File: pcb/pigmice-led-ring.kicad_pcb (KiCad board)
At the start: 2 copper layers, 65 x 56 mm, 37 parts, among them J1 Conn_02x20_Odd_Even, J2 Conn_01x02_Female, U1 TPS61165, U2 LMR33630

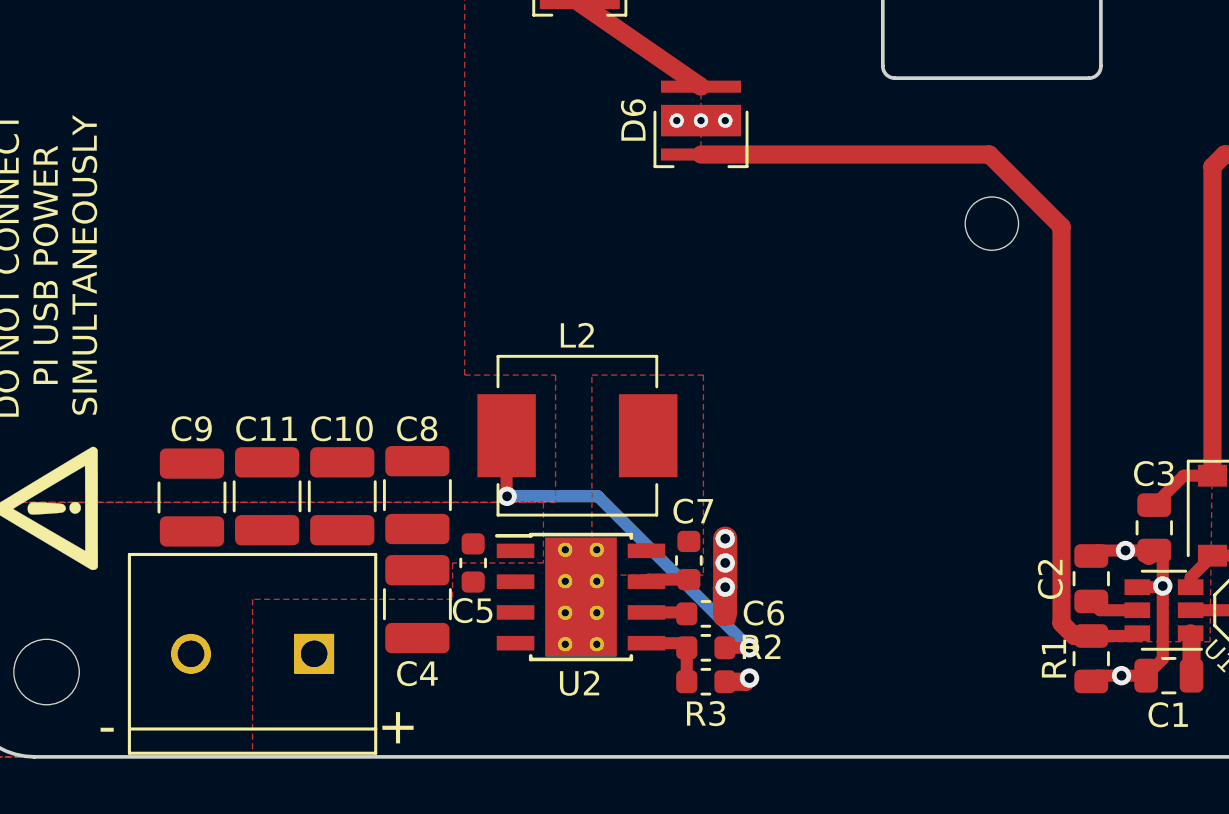
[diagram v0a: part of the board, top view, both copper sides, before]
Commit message: Cleanup PCB
- Order 5v output capacitors
- Don't show J1 and J2 footprints
- Add OSHW logo to the back
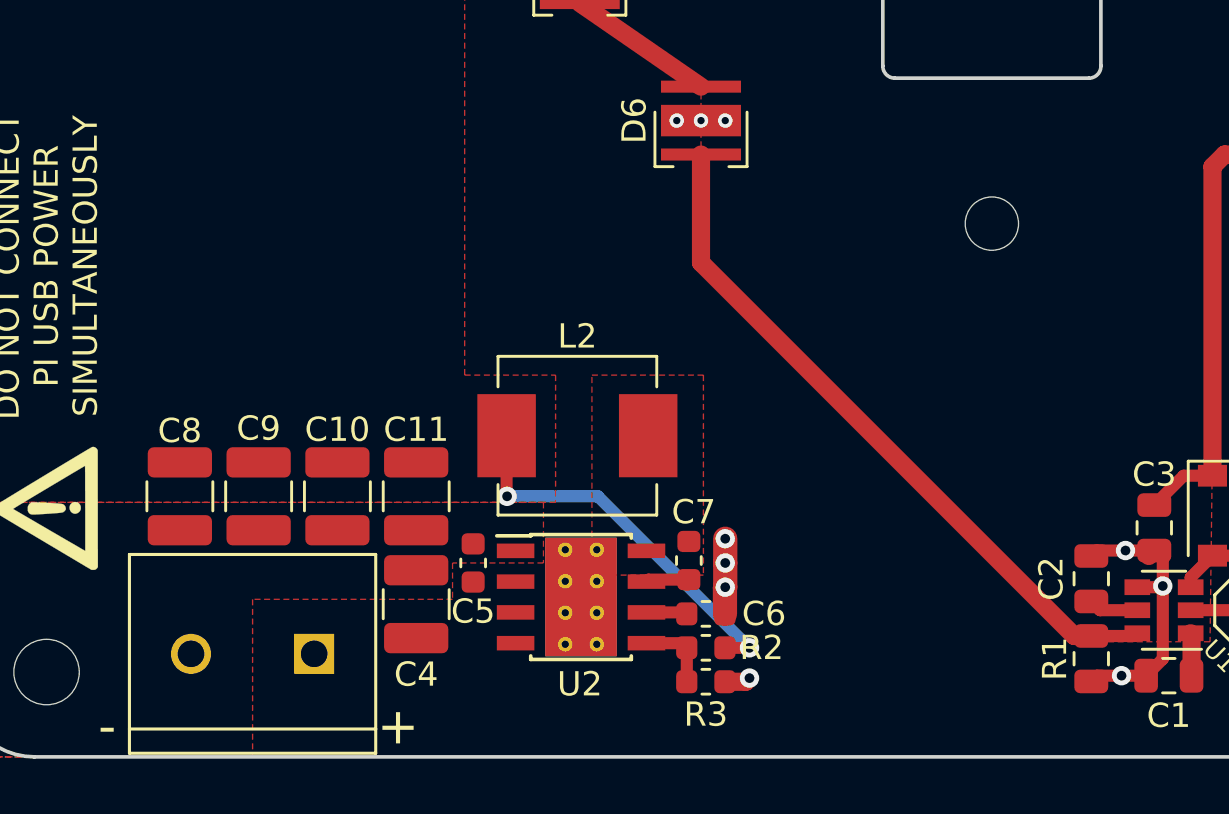
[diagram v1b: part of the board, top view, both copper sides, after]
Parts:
- added REF**: OSHW-Logo2_7.3x6mm_SilkScreen, Symbol:OSHW-Logo2_7.3x6mm_SilkScreen, B.Cu at (154.2, 60.0)
- moved C8 9.80 mm to (159.0, 94.2)
- moved C11 6.15 mm to (168.8, 94.2)
- moved C9 2.75 mm to (162.2, 94.2)
- moved C10 0.20 mm to (165.5, 94.2)
- moved C4 0.05 mm to (168.8, 98.7)
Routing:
- net /FB1: track 35.9 -> 28.9 mm

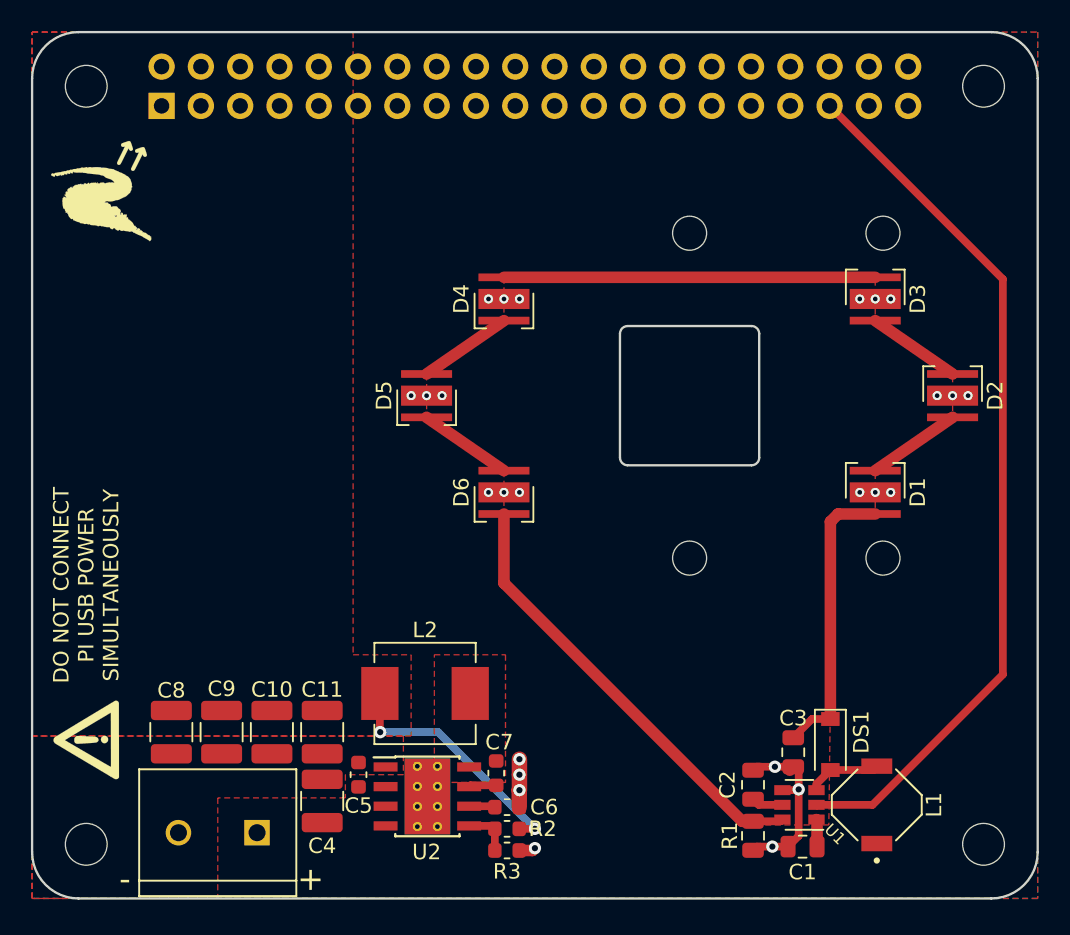
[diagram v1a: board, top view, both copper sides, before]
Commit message: Clean up libraries, schematic, PCB
* Consolidate footprint and symbol libraries
* Fix Cree XP E-2 thermal vias
* GND planes on both sides
* Vpi copper fill on both sides, connected with vias
* No Vbat copper fill, replaced with 1mm trace
* Fix all DRC and ERC errors
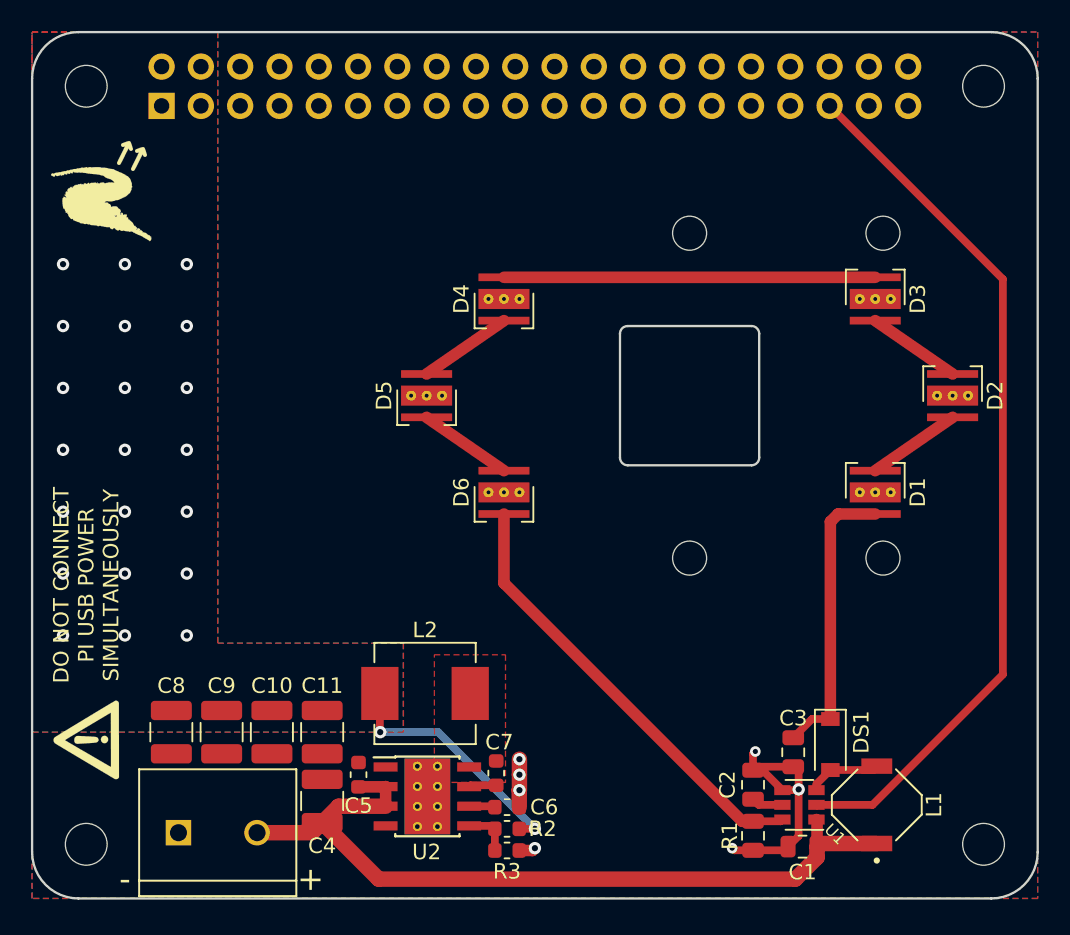
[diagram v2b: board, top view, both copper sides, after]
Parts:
- D1, D2, D3, D4, D5, D6: footprint LED_SMD:LED_Cree-XP -> pigmice-led-ring:LED_Cree-XP
- G***: footprint led-ring:glow_worm_logo -> pigmice-led-ring:glow_worm_logo
- G***: footprint led-ring:warning -> pigmice-led-ring:warning
- J2: footprint led-ring:TE_282837-2 -> pigmice-led-ring:TE_282837-2
- L1: footprint led-ring:IND_#A915AY-100M=P3 -> pigmice-led-ring:IND_#A915AY-100M=P3
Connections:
- J1 pad 1: Net-(J1-Pad1) -> (no net)
- J1 pad 10: Net-(J1-Pad10) -> (no net)
- J1 pad 11: Net-(J1-Pad11) -> (no net)
- J1 pad 12: Net-(J1-Pad12) -> (no net)
- J1 pad 13: Net-(J1-Pad13) -> (no net)
- J1 pad 15: Net-(J1-Pad15) -> (no net)
- J1 pad 16: Net-(J1-Pad16) -> (no net)
- J1 pad 17: Net-(J1-Pad17) -> (no net)
- J1 pad 18: Net-(J1-Pad18) -> (no net)
- J1 pad 19: Net-(J1-Pad19) -> (no net)
- J1 pad 21: Net-(J1-Pad21) -> (no net)
- J1 pad 22: Net-(J1-Pad22) -> (no net)
- J1 pad 23: Net-(J1-Pad23) -> (no net)
- J1 pad 24: Net-(J1-Pad24) -> (no net)
- J1 pad 26: Net-(J1-Pad26) -> (no net)
- J1 pad 27: Net-(J1-Pad27) -> (no net)
- J1 pad 28: Net-(J1-Pad28) -> (no net)
- J1 pad 29: Net-(J1-Pad29) -> (no net)
- J1 pad 3: Net-(J1-Pad3) -> (no net)
- J1 pad 31: Net-(J1-Pad31) -> (no net)
- J1 pad 32: Net-(J1-Pad32) -> (no net)
- J1 pad 33: Net-(J1-Pad33) -> (no net)
- J1 pad 36: Net-(J1-Pad36) -> (no net)
- J1 pad 37: Net-(J1-Pad37) -> (no net)
- J1 pad 38: Net-(J1-Pad38) -> (no net)
- J1 pad 40: Net-(J1-Pad40) -> (no net)
- J1 pad 5: Net-(J1-Pad5) -> (no net)
- J1 pad 7: Net-(J1-Pad7) -> (no net)
- J1 pad 8: Net-(J1-Pad8) -> (no net)
- J2 pad 1: /Vbat -> GND
- J2 pad 2: GND -> /Vbat
- U2 pad 4: Net-(U2-Pad4) -> (no net)
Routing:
- net /Vbat: track 1.77 -> 52.5 mm
- net GND: track 16.2 -> 21.0 mm, vias 25 -> 7
- net /Vpi: vias 2 -> 23
- added copper zone on B.Cu, net /Vpi
- removed copper zone on F.Cu, net (none)
- removed copper zone on F.Cu, net /Vbat

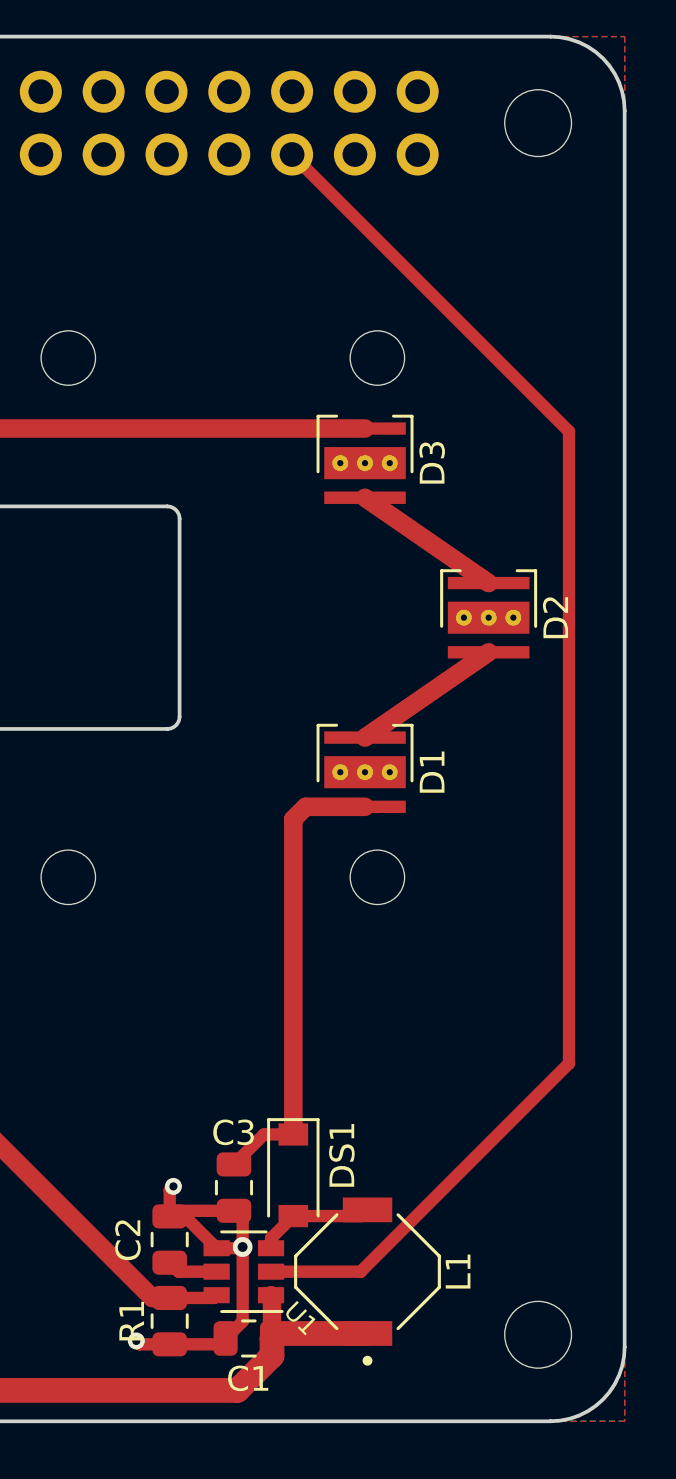
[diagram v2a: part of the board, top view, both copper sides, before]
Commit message: Add DIM pull-down, fixup BOM, zone tolerances
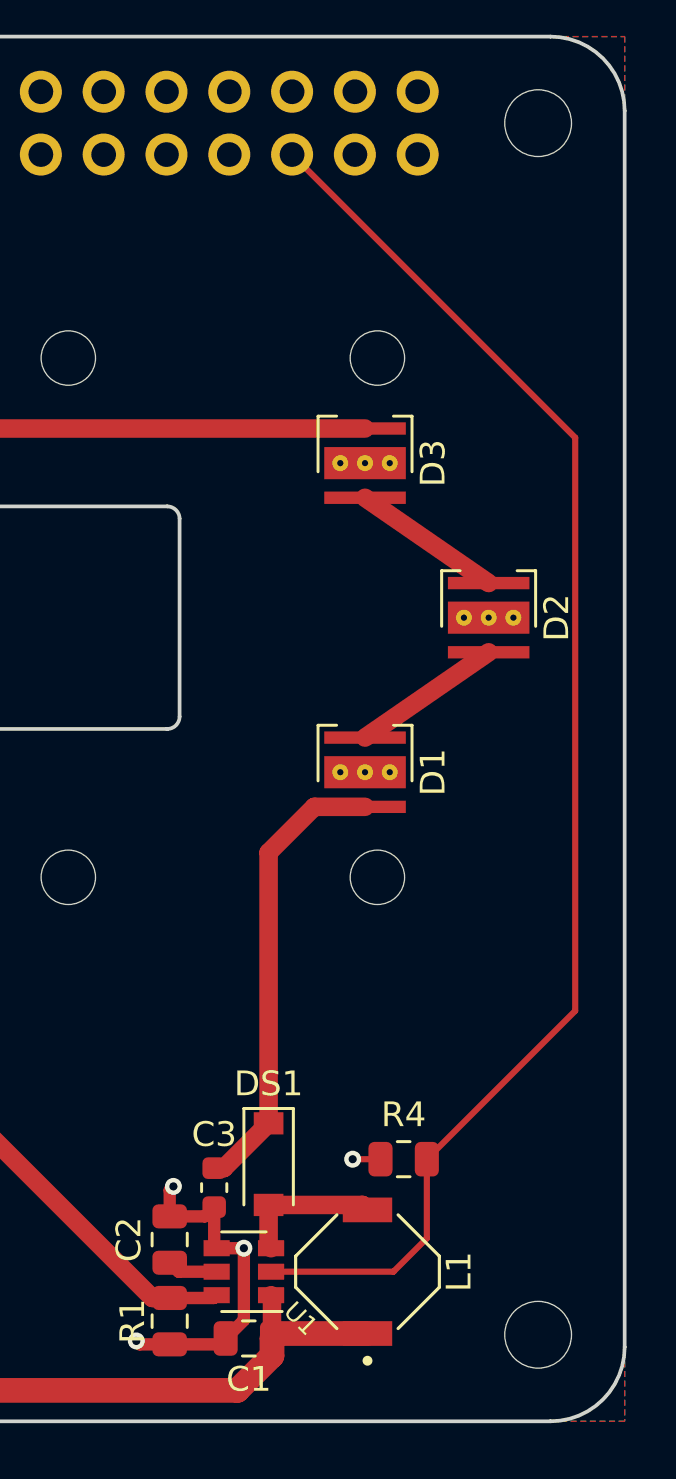
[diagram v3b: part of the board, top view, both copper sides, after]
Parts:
- added R4: 47k, Resistor_SMD:R_0805_2012Metric, F.Cu at (206.1, 94.4)
- C3: footprint Capacitor_SMD:C_0805_2012Metric -> Capacitor_SMD:C_0603_1608Metric
- J1: value Conn_02x20_Odd_Even -> GPIO
- J2: value Conn_01x02_Female -> Power
- moved DS1 1.10 mm to (200.6, 94.6)
- moved C3 0.80 mm to (198.4, 95.5)
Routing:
- net GND: track 21.0 -> 19.1 mm, vias 7 -> 8
- net Net-(DS1-Pad2): track 4.78 -> 5.87 mm
- net /DIM: track 57.4 -> 58.4 mm
